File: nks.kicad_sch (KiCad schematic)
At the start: 18 parts, among them J1 microSD, J2 DevKit-J1, J3 DevKit-J3, SW1 SW_Push, U2 RTC_DS3231+AT24C32, U3 SHT30

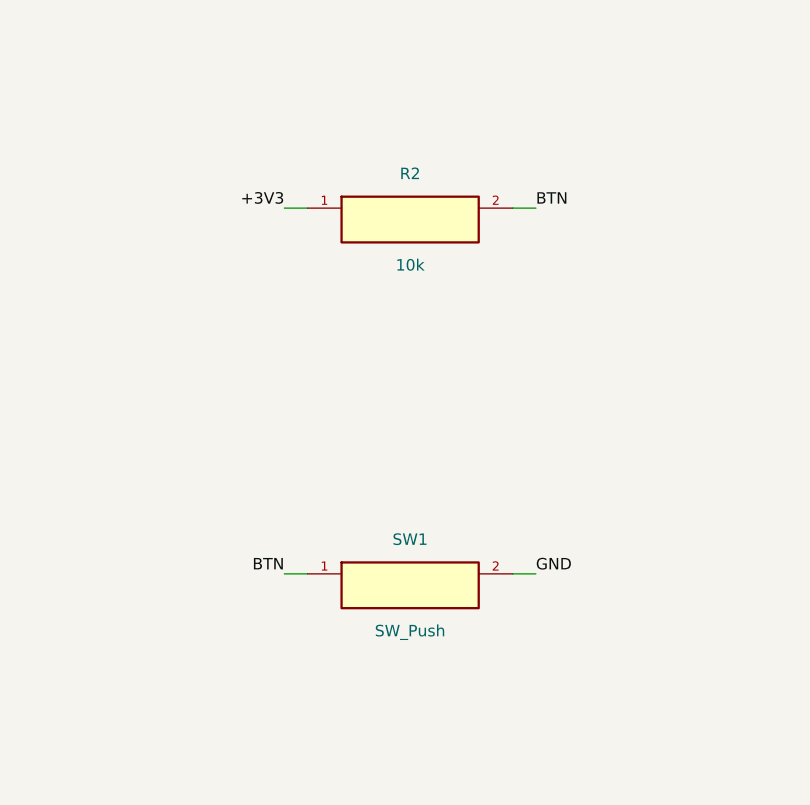
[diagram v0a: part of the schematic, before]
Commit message: feat(sw1): interruptor SPDT (SS12D00) rutado y verificado DRC 0; elimina R2 pull-up; anade libreria de footprints propia nks.pretty
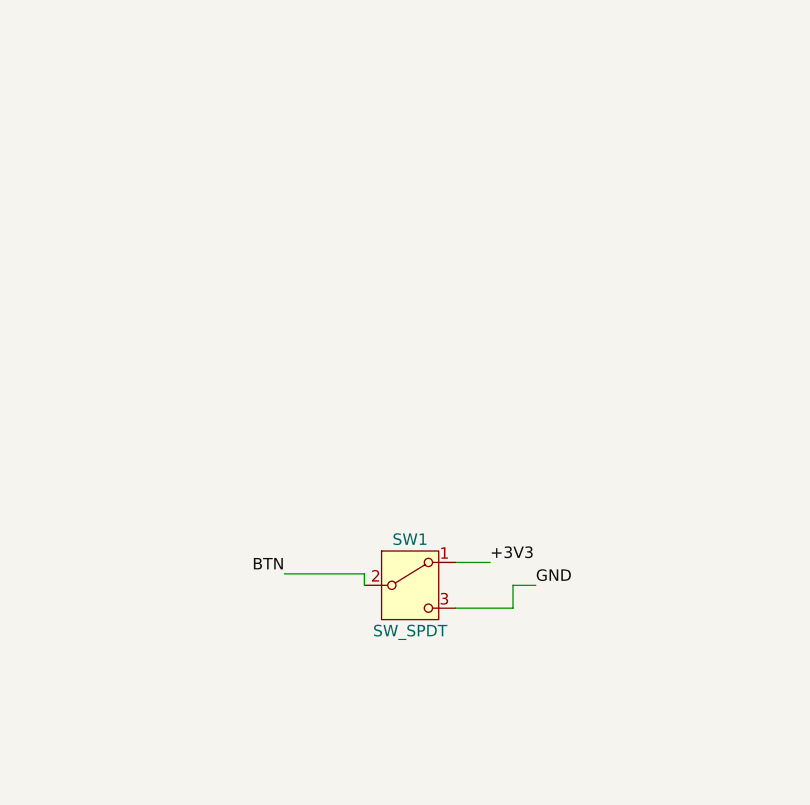
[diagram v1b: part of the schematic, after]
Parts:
- removed R2: 10k, Resistor_SMD:R_0805_2012Metric, symbol nks:R2
- SW1: value SW_Push -> SW_SPDT; footprint Button_Switch_THT:SW_PUSH_6mm -> nks:SS12D00; symbol nks:SW1 -> Switch:SW_SPDT
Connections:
- net +3V3: now also SW1.1 (A)
- net BTN: now also SW1.2 (B); no longer SW1.1
- net GND: now also SW1.3 (C); no longer SW1.2
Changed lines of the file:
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@@
 	(wire
 		(pts
-			(xy 121.92 201.93) (xy 119.38 201.93)
+			(xy 119.38 201.93) (xy 128.27 201.93)
 		)
 		(stroke
@@
 	(wire
 		(pts
-			(xy 144.78 201.93) (xy 147.32 201.93)
+			(xy 144.78 203.2) (xy 147.32 203.2)
 		)
 		(stroke
@@
 	(wire
 		(pts
-			(xy 144.78 161.29) (xy 147.32 161.29)
-		)
-		(stroke
-			(width 0)
-			(type default)
-		)
-	)
-	(wire
-		(pts
 			(xy 294.64 163.83) (xy 297.18 163.83)
 		)
@@
 	(wire
 		(pts
+			(xy 128.27 201.93) (xy 128.27 203.2)
+		)
+		(stroke
+			(width 0)
+			(type default)
+		)
+	)
+	(wire
+		(pts
 			(xy 82.55 46.99) (xy 80.01 46.99)
 		)
@@
 	(wire
 		(pts
+			(xy 138.43 200.66) (xy 142.24 200.66)
+		)
+		(stroke
+			(width 0)
+			(type default)
+		)
+	)
+	(wire
+		(pts
 			(xy 82.55 111.76) (xy 80.01 111.76)
 		)
@@
 	(wire
 		(pts
+			(xy 138.43 205.74) (xy 144.78 205.74)
+		)
+		(stroke
+			(width 0)
+			(type default)
+		)
+	)
+	(wire
+		(pts
 			(xy 105.41 49.53) (xy 107.95 49.53)
 		)
@@
 	(wire
 		(pts
-			(xy 121.92 161.29) (xy 119.38 161.29)
-		)
-		(stroke
-			(width 0)
-			(type default)
-		)
-	)
-	(wire
-		(pts
 			(xy 191.77 242.57) (xy 189.23 242.57)
 		)
@@
 		(pts
 			(xy 82.55 114.3) (xy 80.01 114.3)
+		)
+		(stroke
+			(width 0)
+			(type default)
+		)
+	)
+	(wire
+		(pts
+			(xy 144.78 205.74) (xy 144.78 203.2)
 		)
 		(stroke
@@
 		)
 	)
+	(label "+3V3"
+		(at 142.24 200.66 0)
+		(effects
+			(font
+				(size 1.27 1.27)
+			)
+			(justify left bottom)
+		)
+	)
 	(label "GND"
 		(at 189.23 44.45 180)
@@
 		)
 	)
-	(label "BTN"
-		(at 147.32 161.29 0)
-		(effects
-			(font
-				(size 1.27 1.27)
-			)
-			(justify left bottom)
-		)
-	)
 	(label "SD_MOSI"
 		(at 107.95 41.91 0)
@@
 		)
 	)
-	(label "+3V3"
-		(at 119.38 161.29 180)
-		(effects
-			(font
-				(size 1.27 1.27)
-			)
-			(justify right bottom)
-		)
-	)
 	(label "SD_CS"
 		(at 107.95 49.53 0)
@@
 	)
 	(label "GND"
-		(at 147.32 201.93 0)
+		(at 147.32 203.2 0)
 		(effects
 			(font
@@
 	)
 	(symbol
-		(lib_id "nks:R2")
-		(at 133.35 162.56 0)
-		(unit 1)
-		(body_style 1)
-		(exclude_from_sim no)
-		(in_bom yes)
-		(on_board yes)
-		(in_pos_files yes)
-		(dnp no)
-		(property "Reference" "R2"
-			(at 133.35 157.48 0)
-			(show_name no)
-			(do_not_autoplace no)
-			(effects
-				(font
-					(size 1.27 1.27)
-				)
-			)
-		)
-		(property "Value" "10k"
-			(at 133.35 167.64 0)
-			(show_name no)
-			(do_not_autoplace no)
-			(effects
-				(font
-					(size 1.27 1.27)
-				)
-			)
-		)
-		(property "Footprint" "Resistor_SMD:R_0805_2012Metric"
-			(at 133.35 162.56 0)
-			(hide yes)
-			(show_name no)
-			(do_not_autoplace no)
-			(effects
-				(font
-					(size 1.27 1.27)
-				)
-			)
-		)
-		(property "Datasheet" ""
-			(at 133.35 162.56 0)
-			(show_name no)
-			(do_not_autoplace no)
-			(effects
-				(font
-					(size 1.27 1.27)
-				)
-			)
-		)
-		(property "Description" ""
-			(at 133.35 162.56 0)
-			(show_name no)
-			(do_not_autoplace no)
-			(effects
-				(font
-					(size 1.27 1.27)
-				)
-			)
-		)
-		(pin "1"
-		)
-		(pin "2"
-		)
-		(instances
-			(project "nks"
-				(path "/ff07ce8f-c3d4-45e3-8c6f-5cb7c24c6ede"
-					(reference "R2")
-					(unit 1)
-				)
-			)
-		)
-	)
-	(symbol
 		(lib_id "nks:J3")
 		(at 93.98 114.3 0)
@@
 	)
 	(symbol
-		(lib_id "nks:SW1")
+		(lib_id "Switch:SW_SPDT")
 		(at 133.35 203.2 0)
 		(unit 1)
@@
 			)
 		)
-		(property "Value" "SW_Push"
+		(property "Value" "SW_SPDT"
 			(at 133.35 208.28 0)
 			(show_name no)
@@
 			)
 		)
-		(property "Footprint" "Button_Switch_THT:SW_PUSH_6mm"
+		(property "Footprint" "nks:SS12D00"
 			(at 133.35 203.2 0)
 			(hide yes)
@@
 		)
 		(property "Datasheet" ""
+			(at 133.35 210.82 0)
+			(hide yes)
+			(show_name no)
+			(do_not_autoplace no)
+			(effects
+				(font
+					(size 1.27 1.27)
+				)
+			)
+		)
+		(property "Description" "Switch, single pole double throw"
 			(at 133.35 203.2 0)
-			(show_name no)
-			(do_not_autoplace no)
-			(effects
-				(font
-					(size 1.27 1.27)
-				)
-			)
-		)
-		(property "Description" ""
-			(at 133.35 203.2 0)
-			(show_name no)
-			(do_not_autoplace no)
-			(effects
-				(font
-					(size 1.27 1.27)
+			(hide yes)
+			(show_name no)
+			(do_not_autoplace no)
+			(effects
+				(font
+					(size 1.27 1.27)
+					(thickness 0.254)
+					(bold yes)
 				)
 			)
@@
 		(pin "2"
 		)
+		(pin "3"
+		)
 		(instances

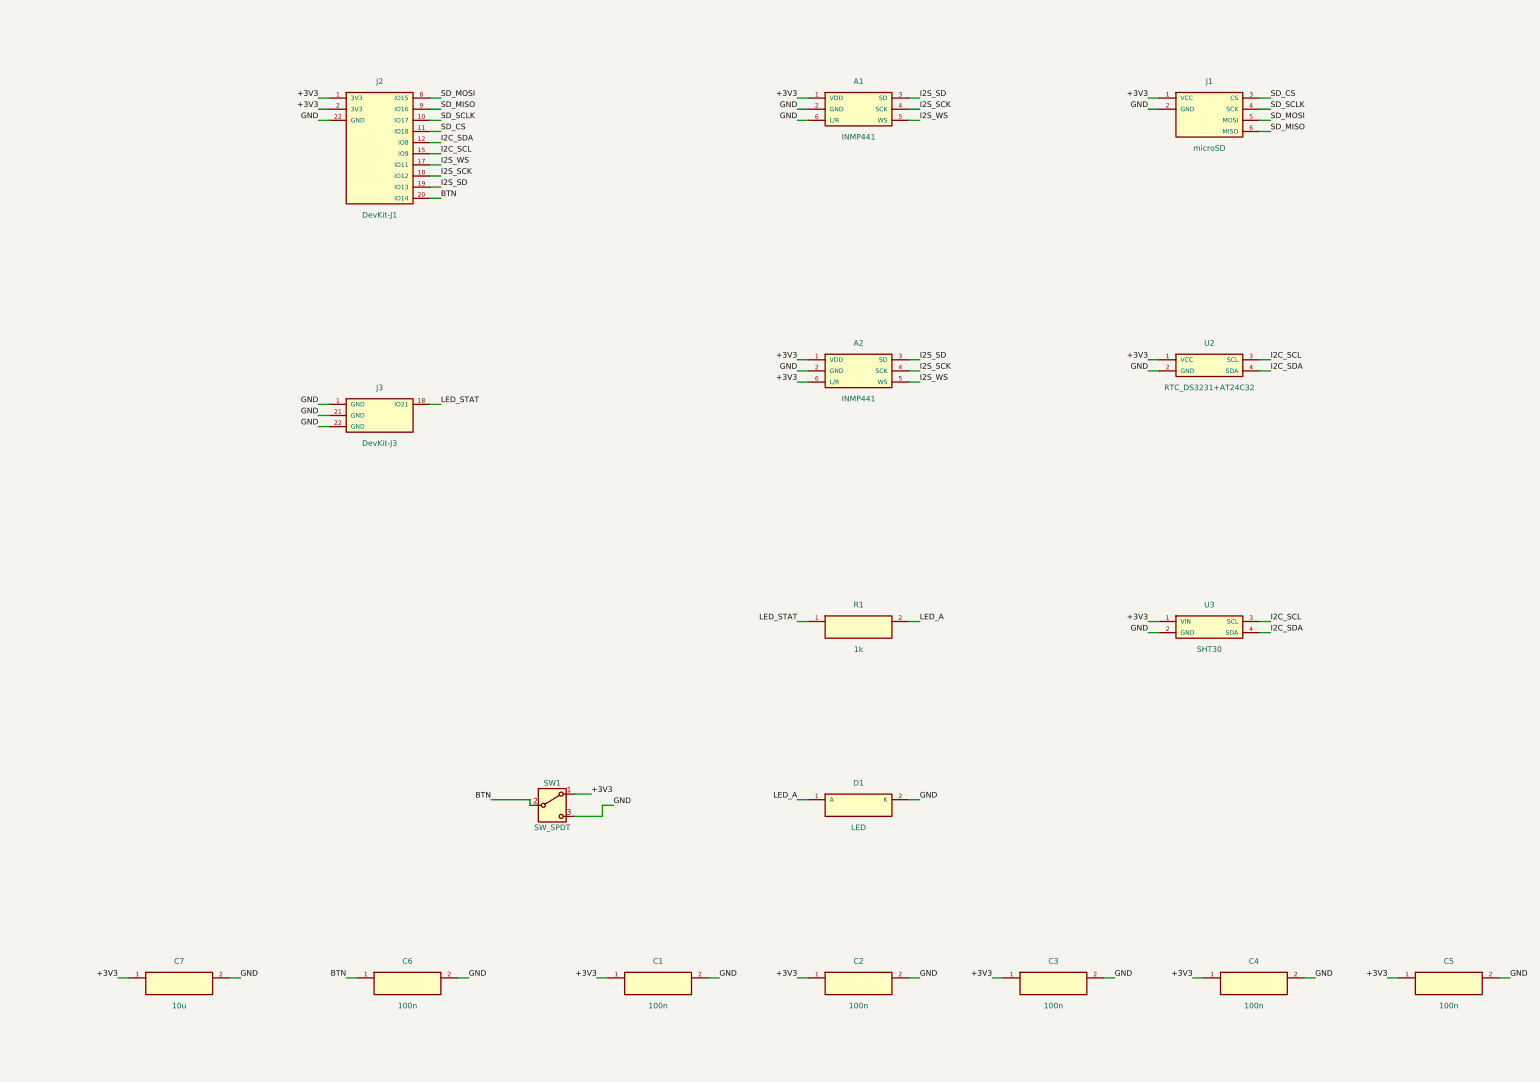
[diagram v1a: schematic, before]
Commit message: layout: reconstruccion PCB desde esquematico nuevo - 20 componentes colocados, DevKit orientado USB trasero, panel LED+switch frontal
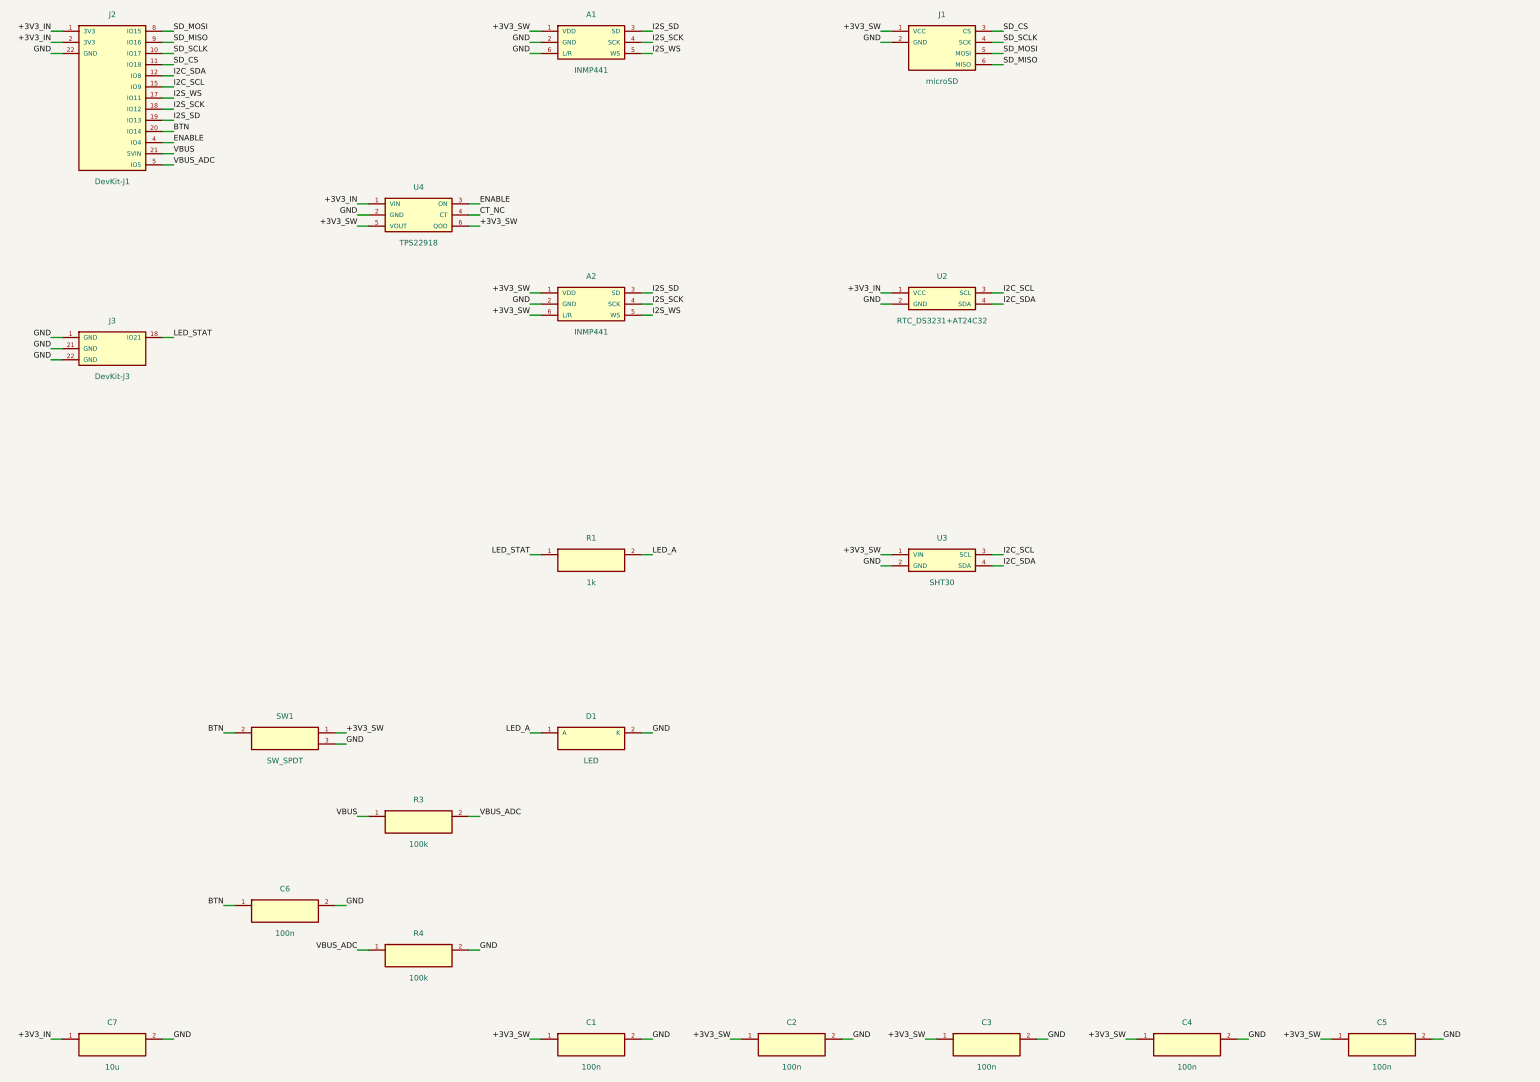
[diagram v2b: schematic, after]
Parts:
- removed SW1: SW_SPDT, nks:SS12D00, symbol Switch:SW_SPDT
- added R3: 100k, Resistor_SMD:R_0805_2012Metric, symbol nks:R3
- added R4: 100k, Resistor_SMD:R_0805_2012Metric, symbol nks:R4
- added SW1: SW_SPDT, nks:SS12D00, symbol nks:SW1
- added U4: TPS22918, Package_TO_SOT_SMD:SOT-23-6, symbol nks:U4
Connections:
- net BTN: now also SW1.2
- net GND: now also R4.2, SW1.3, U4.2 (GND)
- net +3V3 renamed +3V3_SW
- net +3V3_SW: now also SW1.1, U4.5 (VOUT), U4.6 (QOD); no longer C7.1, J2.1 (3V3), J2.2 (3V3), U2.1 (VCC)
- new net +3V3_IN: C7.1, J2.1 (3V3), J2.2 (3V3), U2.1 (VCC), U4.1 (VIN)
- new net CT_NC: U4.4 (CT)
- new net ENABLE: J2.4 (IO4), U4.3 (ON)
- new net VBUS: J2.21 (5VIN), R3.1
- new net VBUS_ADC: J2.5 (IO5), R3.2, R4.1
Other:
- moved on the sheet: A1, A2, C1, C2, C3, C4, C5, C6, C7, D1, J1, J3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

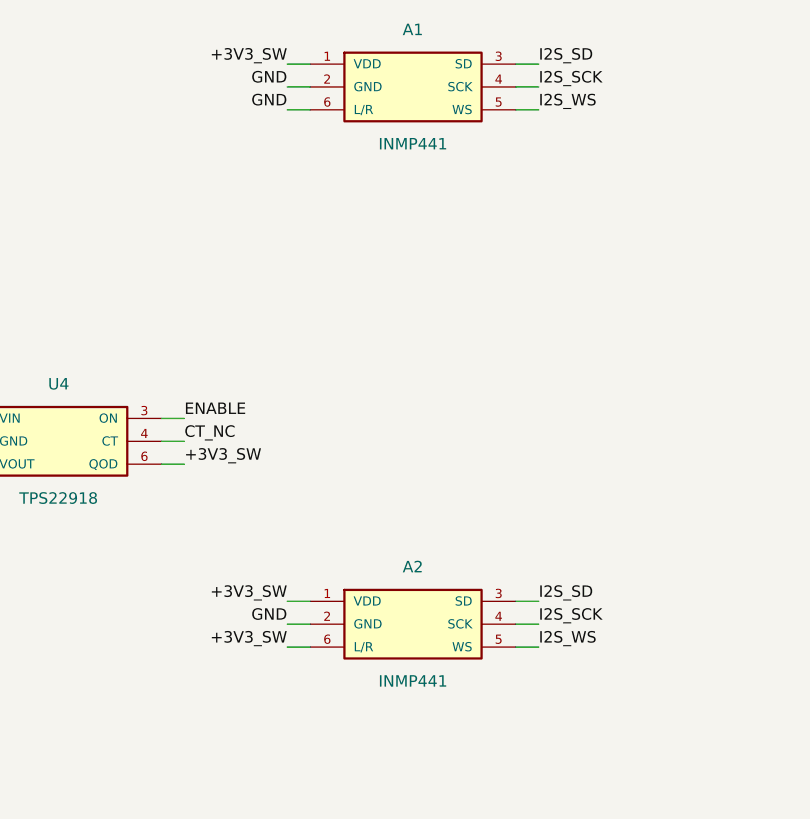
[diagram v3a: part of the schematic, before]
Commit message: fix(micros): footprint A1/A2 corregido de 1x06 a 2x03 (INMP441 real) + mapeo pines 1=L/R,2=GND,3=WS,4=VDD,5=SCK,6=SD
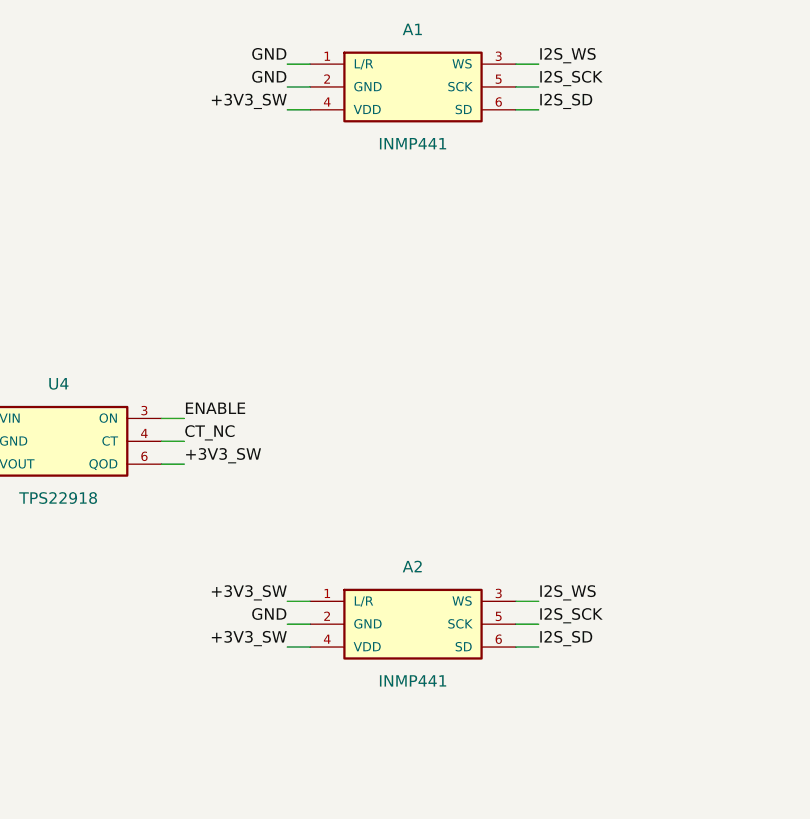
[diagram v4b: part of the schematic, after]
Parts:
- A1, A2: footprint Connector_PinHeader_2.54mm:PinHeader_1x06_P2.54mm_Vertical -> Connector_PinHeader_2.54mm:PinHeader_2x03_P2.54mm_Vertical
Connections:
- net +3V3_SW: now also A1.4 (VDD), A2.4 (VDD); no longer A1.1 (VDD), A2.6 (L/R)
- net GND: now also A1.1 (L/R); no longer A1.6 (L/R)
- net I2S_SCK: now also A1.5 (SCK), A2.5 (SCK); no longer A1.4 (SCK), A2.4 (SCK)
- net I2S_SD: now also A1.6 (SD), A2.6 (SD); no longer A1.3 (SD), A2.3 (SD)
- net I2S_WS: now also A1.3 (WS), A2.3 (WS); no longer A1.5 (WS), A2.5 (WS)
